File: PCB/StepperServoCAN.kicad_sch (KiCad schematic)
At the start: 134 parts, among them J1 CAR, J2 Debug, J3 Motor, J4 Conn_01x06, Q1 AO3401A, Q2 2N7002, Q3 AO3401A, SW1 Rst, SW2 Fcn>, SW3 Fcn>, U2 STM32F103CBT6, U3 LMV321, U4 AT8236, U5 DRV8870, U6 LMV321, U7 TLE5012B, U8 TMAG5170-Q1, U9 SN65HVD230, Y1 16Mhz 9pF

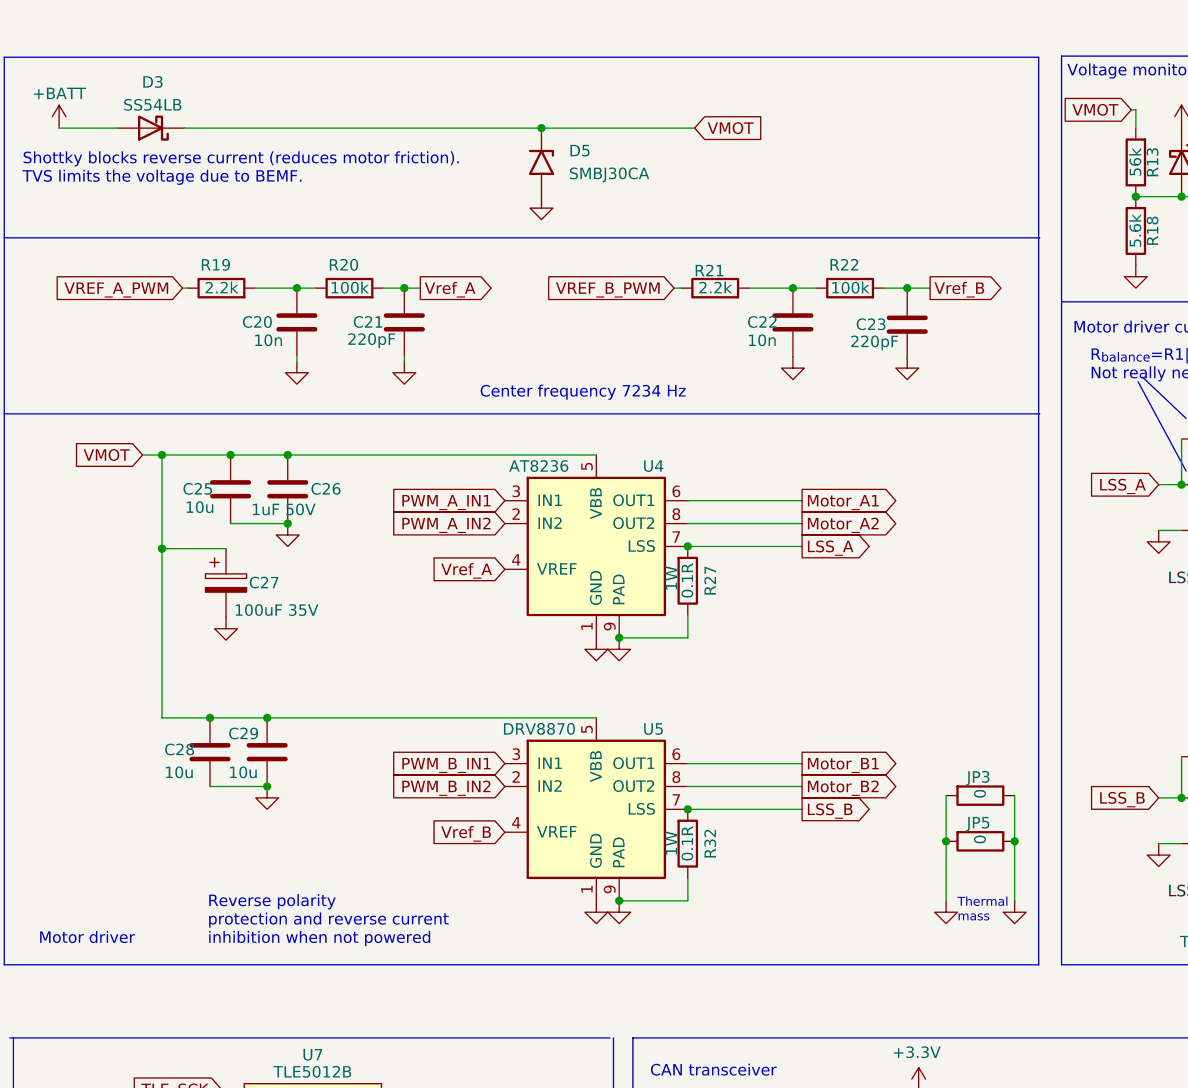
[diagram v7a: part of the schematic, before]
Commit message: More powerful and lower breakdown voltage SMCJ28CA TVS. Better component placement - more ground pour. Capacitors moved away from mounting hole to avoid cracking
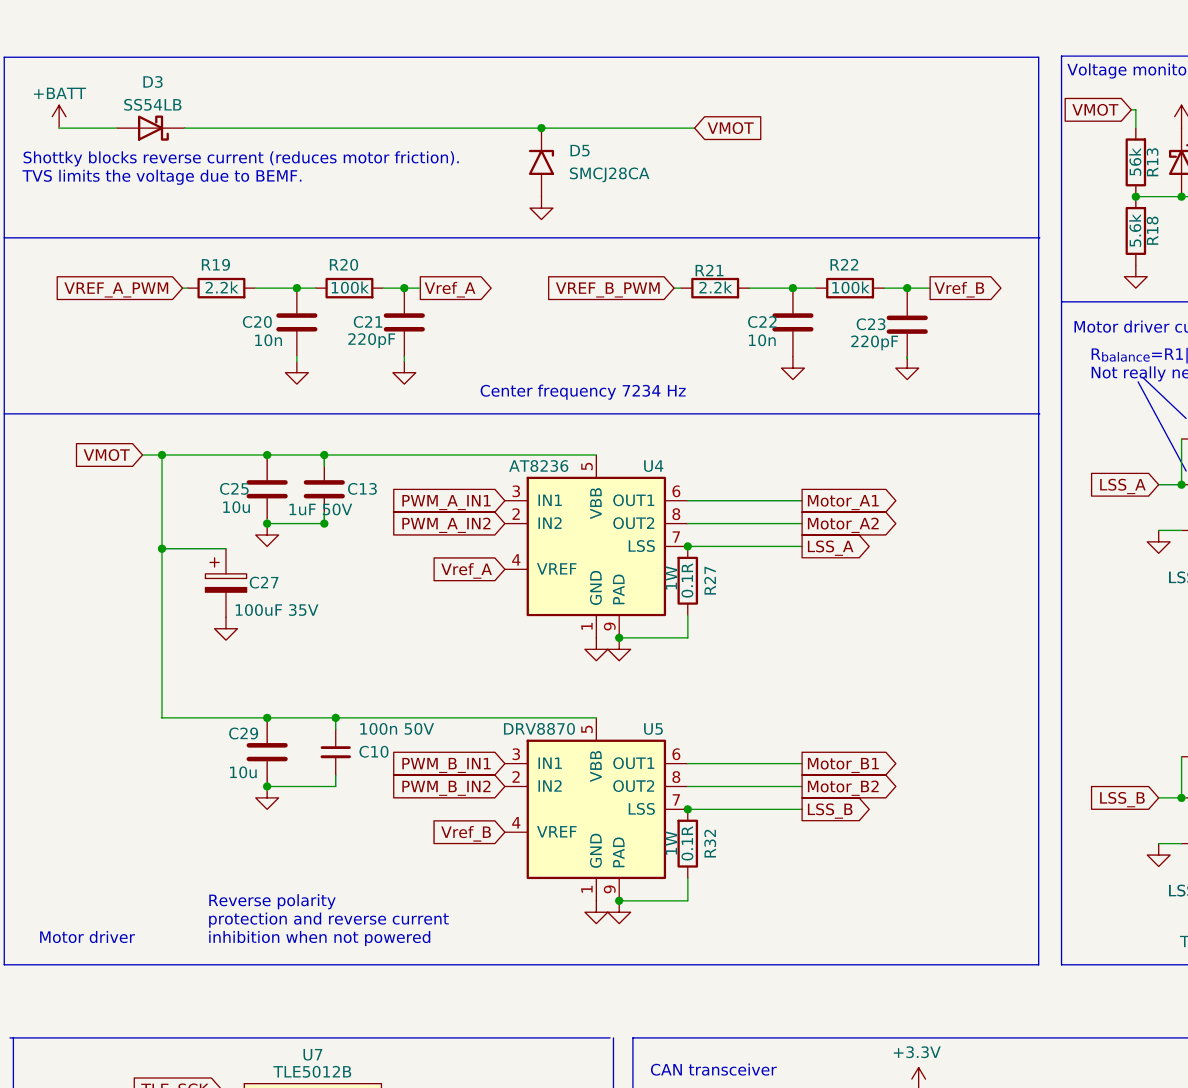
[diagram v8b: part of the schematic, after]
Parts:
- removed C26: 1uF 50V, Capacitor_SMD:C_0805_2012Metric, symbol Device:C
- removed C28: 10u, Capacitor_SMD:C_1206_3216Metric, symbol Device:C
- removed JP3, JP5: 0, Resistor_SMD:R_0603_1608Metric, symbol Device:R
- added C10: 100n 50V, Capacitor_SMD:C_0402_1005Metric, symbol Device:C_Small
- added C13: 1uF 50V, Capacitor_SMD:C_0805_2012Metric, symbol Device:C
- C29: footprint Capacitor_SMD:C_1206_3216Metric_Pad1.33x1.80mm_HandSolder -> Capacitor_SMD:C_1206_3216Metric
- D5: value SMBJ30CA -> SMCJ28CA; footprint Diode_SMD:D_SMB -> Diode_SMD:D_SMC; LCSC C2925441 -> C19077606
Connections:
- net GND: now also C10.2, C13.2
- net VMOT: now also C10.1, C13.1
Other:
- note removed: "Thermal mass"
- moved on the sheet: C25
